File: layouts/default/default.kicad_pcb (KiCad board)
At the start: 2 copper layers, 27 parts

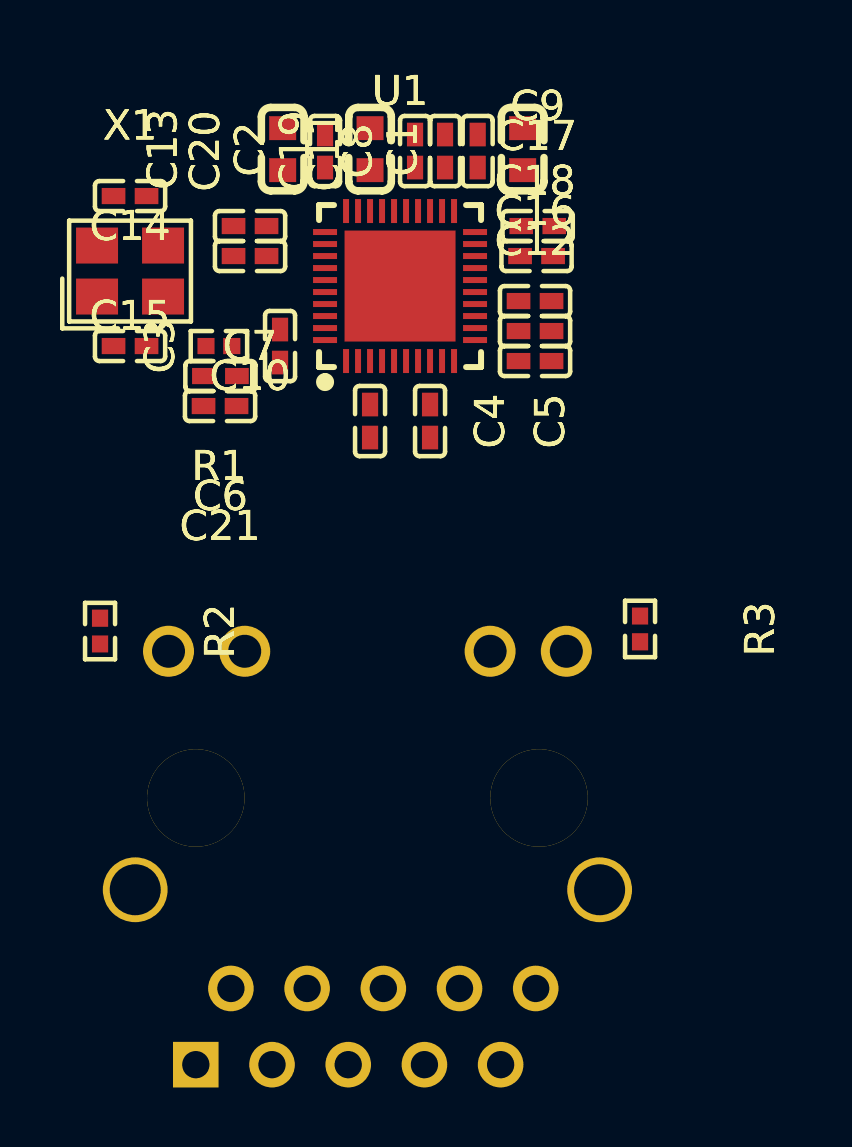
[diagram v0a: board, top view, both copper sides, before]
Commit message: Renamed the module and adjusted the layout.
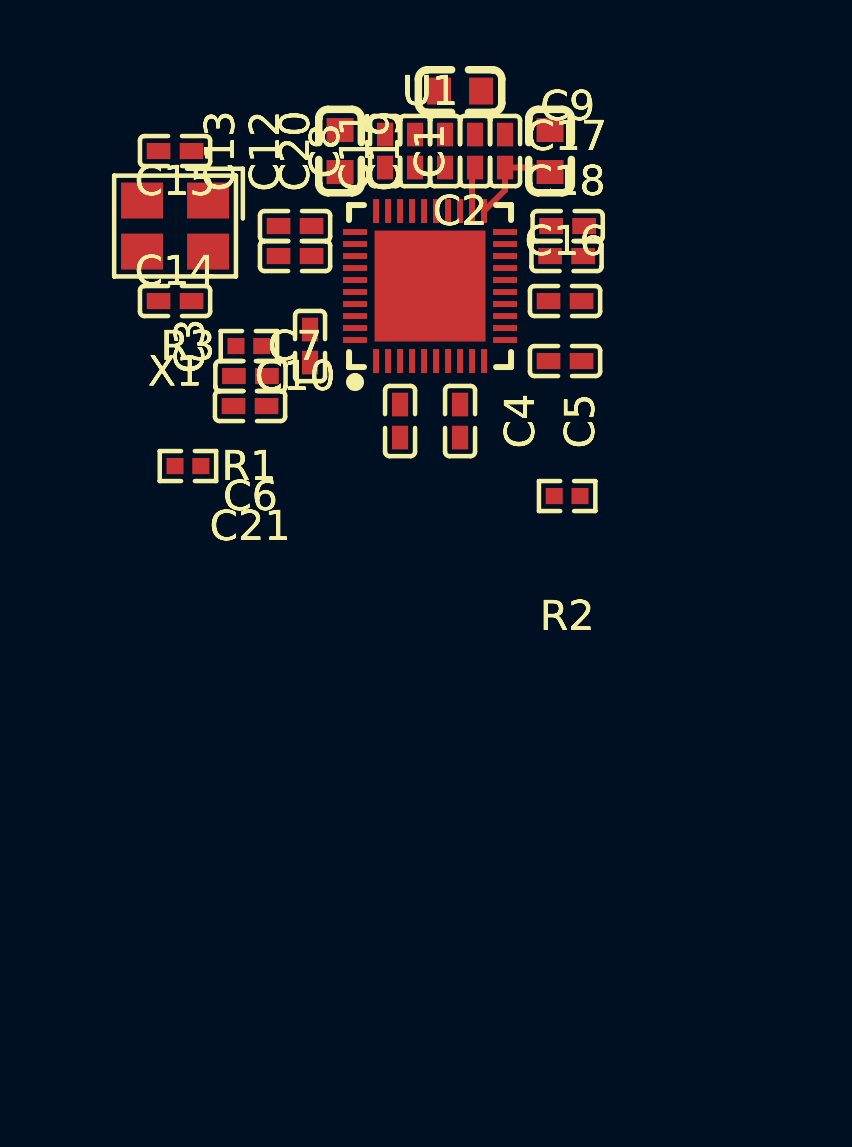
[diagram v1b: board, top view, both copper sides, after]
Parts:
- removed RJ1: , HANRUN_HR911130A:RJ45-TH_HR911130A
- moved R2 16.2 mm to (113.1, 120.5), turned to 180 degrees
- moved R3 16.0 mm to (100.4, 119.5), turned to 0 degrees
- moved C12 8.60 mm to (107.0, 109.0), turned to 90 degrees
- moved C14 6.67 mm to (100.0, 109.0), turned to 180 degrees
- moved C15 3.81 mm to (100.0, 114.0), turned to 0 degrees
- moved C2 3.57 mm to (109.5, 107.0), turned to 180 degrees
- moved C19 3.00 mm to (111.0, 109.0)
- moved C20 3.00 mm to (108.0, 109.0)
- moved X1 2.12 mm to (100.0, 111.5), turned to 180 degrees
- moved C13 1.91 mm to (105.5, 109.0)
- moved C10 1.50 mm to (104.0, 112.5)
- moved C7 1.50 mm to (104.0, 111.5)
- moved C16 1.41 mm to (113.0, 116.0)
- moved C8 1.09 mm to (109.0, 109.0)
- moved C11 1.00 mm to (110.0, 109.0)
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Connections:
- U1 pad 1: MDI0pos -> MDI0_P
- U1 pad 10: MDI3neg -> MDI3_N
- U1 pad 2: MDI0neg -> MDI0_N
- U1 pad 4: MDI1pos -> MDI1_P
- U1 pad 5: MDI1neg -> MDI1_N
- U1 pad 6: MDI2pos -> MDI2_P
- U1 pad 7: MDI2neg -> MDI2_N
- U1 pad 9: MDI3pos -> MDI3_P
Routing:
- net power_5v-VCC: track 0.00 -> 3.30 mm
- net DVDD10_UPS: track 0.00 -> 1.49 mm
